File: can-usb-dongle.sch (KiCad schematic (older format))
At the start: 42 parts, among them SW1 SW_PUSH, U1 STM32F302C8T, U2 SN65HVD256, U3 NUF2042XV6, U4 MCP1700, U5 SiP32431, X1 16MHz 10ppm

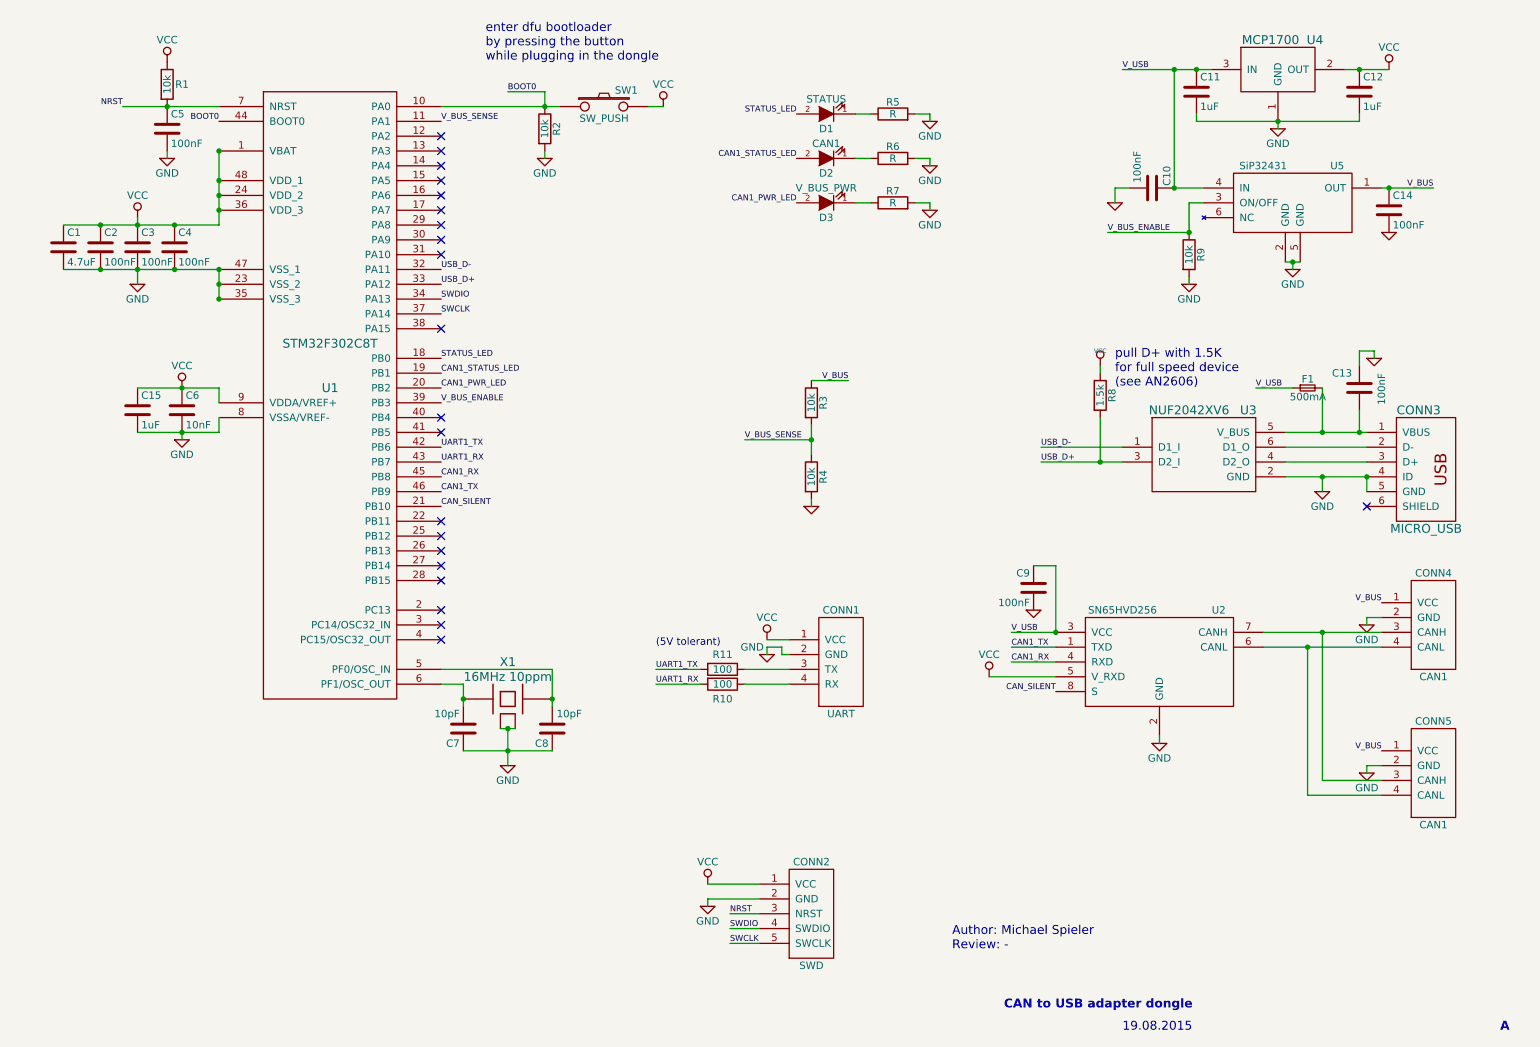
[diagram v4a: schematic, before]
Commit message: Change pinout to optimize routing.
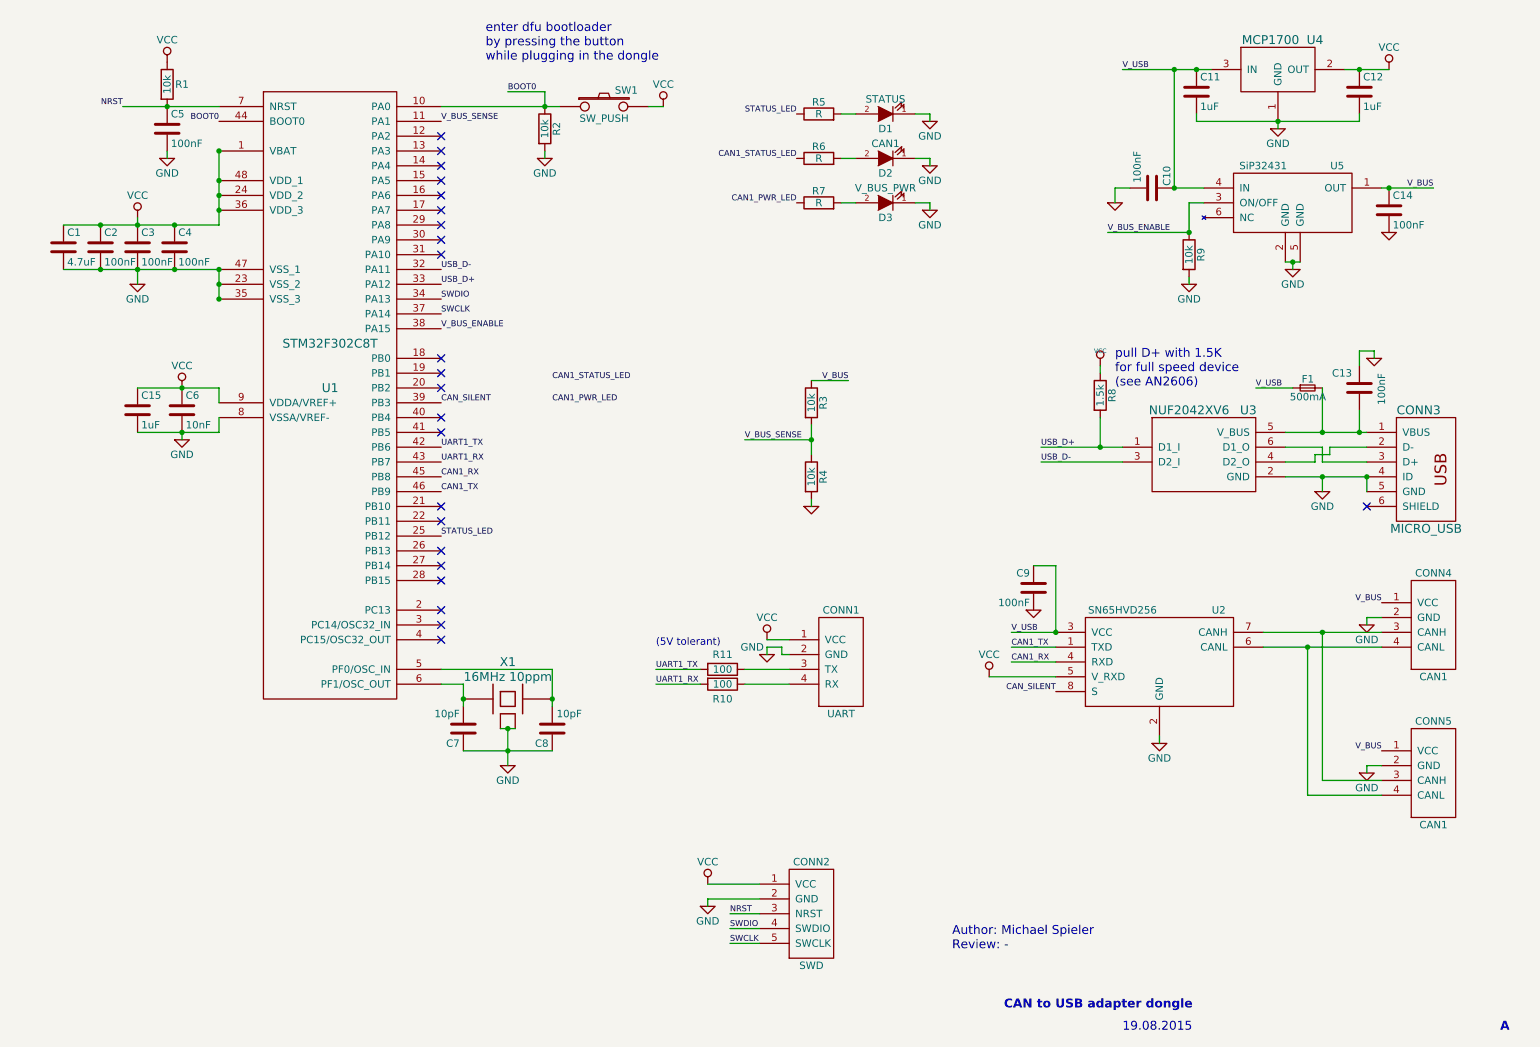
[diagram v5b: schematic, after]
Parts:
- CONN3: footprint _connectors:_Micro-USB-AB-receptacle-SMT-th -> _connectors:_Micro-USB-AB-receptacle-SMT-th-no-slot
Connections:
- net CAN1_PWR_LED: now also R7.1; no longer D3.2 (A), U1.20 (PB2)
- net CAN1_STATUS_LED: now also R6.1; no longer D2.2 (A), U1.19 (PB1)
- net CAN_SILENT: now also U1.39 (PB3); no longer U1.21 (PB10)
- net GND: now also D1.1 (K), D2.1 (K), D3.1 (K); no longer R5.2, R6.2, R7.2
- net STATUS_LED: now also R5.1, U1.25 (PB12); no longer D1.2 (A), U1.18 (PB0)
- net USB_D+: now also U3.1 (D1_I); no longer U3.3 (D2_I)
- net USB_D-: now also U3.3 (D2_I); no longer U3.1 (D1_I)
- net V_BUS_ENABLE: now also U1.38 (PA15); no longer U1.39 (PB3)
- net at CONN3.2 (D-): now also U3.4 (D2_O); no longer U3.6 (D1_O)
- net at CONN3.3 (D+): now also U3.6 (D1_O); no longer U3.4 (D2_O)
- new net: D2.2 (A), R6.2
- new net: D1.2 (A), R5.2
- new net: D3.2 (A), R7.2
- no-connect marks 21 -> 23
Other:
- moved on the sheet: D1, D2, D3, R5, R6, R7
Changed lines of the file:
@@
 Text Label 3600 2600 0    40   ~ 0
 USB_D+
+Text Label 7650 3800 0    40   ~ 0
+USB_D-
 Text Label 7650 3700 0    40   ~ 0
-USB_D-
-Text Label 7650 3800 0    40   ~ 0
 USB_D+
 Text Label 9100 3300 0    40   ~ 0
@@
 L R R6
 U 1 1 55622F4C
-P 6650 1750
-F 0 "R6" V 6730 1750 50  0000 C CNN
-F 1 "R" V 6650 1750 50  0000 C CNN
-F 2 "_std:_0603" V 6580 1750 30  0001 C CNN
-F 3 "" H 6650 1750 30  0000 C CNN
-	1    6650 1750
+P 6150 1750
+F 0 "R6" V 6230 1750 50  0000 C CNN
+F 1 "R" V 6150 1750 50  0000 C CNN
+F 2 "_std:_0603" V 6080 1750 30  0001 C CNN
+F 3 "" H 6150 1750 30  0000 C CNN
+	1    6150 1750
 	0    -1   -1   0
 $EndComp
@@
 L LED D1
 U 1 1 55624274
-P 6200 1450
-F 0 "D1" H 6200 1550 50  0000 C CNN
-F 1 "STATUS" H 6200 1350 50  0000 C CNN
-F 2 "_std:_0603" H 6200 1450 60  0001 C CNN
-F 3 "" H 6200 1450 60  0000 C CNN
-	1    6200 1450
+P 6600 1450
+F 0 "D1" H 6600 1550 50  0000 C CNN
+F 1 "STATUS" H 6600 1350 50  0000 C CNN
+F 2 "_std:_0603" H 6600 1450 60  0001 C CNN
+F 3 "" H 6600 1450 60  0000 C CNN
+	1    6600 1450
 	-1   0    0    1
 $EndComp
@@
 L R R5
 U 1 1 5562427A
-P 6650 1450
-F 0 "R5" V 6730 1450 50  0000 C CNN
-F 1 "R" V 6650 1450 50  0000 C CNN
-F 2 "_std:_0603" V 6580 1450 30  0001 C CNN
-F 3 "" H 6650 1450 30  0000 C CNN
-	1    6650 1450
+P 6150 1450
+F 0 "R5" V 6230 1450 50  0000 C CNN
+F 1 "R" V 6150 1450 50  0000 C CNN
+F 2 "_std:_0603" V 6080 1450 30  0001 C CNN
+F 3 "" H 6150 1450 30  0000 C CNN
+	1    6150 1450
 	0    -1   -1   0
 $EndComp
@@
 Text Label 6000 1450 2    40   ~ 0
 STATUS_LED
-Text Label 3600 3200 0    40   ~ 0
+Text Label 4350 3250 0    40   ~ 0
 CAN1_STATUS_LED
 $Comp
 L LED D2
 U 1 1 55622E77
-P 6200 1750
-F 0 "D2" H 6200 1850 50  0000 C CNN
-F 1 "CAN1" H 6200 1650 50  0000 C CNN
-F 2 "_std:_0603" H 6200 1750 60  0001 C CNN
-F 3 "" H 6200 1750 60  0000 C CNN
-	1    6200 1750
+P 6600 1750
+F 0 "D2" H 6600 1850 50  0000 C CNN
+F 1 "CAN1" H 6600 1650 50  0000 C CNN
+F 2 "_std:_0603" H 6600 1750 60  0001 C CNN
+F 3 "" H 6600 1750 60  0000 C CNN
+	1    6600 1750
 	-1   0    0    1
 $EndComp
@@
 	1    0    0    -1
 $EndComp
-Text Label 7450 4950 0    40   ~ 0
-V_USB
 $Comp
 L VCC #PWR018
@@
 	1    0    0    -1
 $EndComp
-Text Label 3600 4100 0    40   ~ 0
+Text Label 3600 3400 0    40   ~ 0
 CAN_SILENT
 Text Label 3600 3800 0    40   ~ 0
@@
 Text Label 3600 3700 0    40   ~ 0
 UART1_TX
-Text Label 3600 3100 0    40   ~ 0
+Text Label 3600 4300 0    40   ~ 0
 STATUS_LED
 Text Notes 3900 1100 0    60   ~ 0
@@
 Text Label 8100 2250 0    40   ~ 0
 V_BUS_ENABLE
-Text Label 3600 3400 0    40   ~ 0
+Text Label 3600 2900 0    40   ~ 0
 V_BUS_ENABLE
 $Comp
@@
 L LED D3
 U 1 1 560BDA9A
-P 6200 2050
-F 0 "D3" H 6200 2150 50  0000 C CNN
-F 1 "V_BUS_PWR" H 6200 1950 50  0000 C CNN
-F 2 "_std:_0603" H 6200 2050 60  0001 C CNN
-F 3 "" H 6200 2050 60  0000 C CNN
-	1    6200 2050
+P 6600 2050
+F 0 "D3" H 6600 2150 50  0000 C CNN
+F 1 "V_BUS_PWR" H 6600 1950 50  0000 C CNN
+F 2 "_std:_0603" H 6600 2050 60  0001 C CNN
+F 3 "" H 6600 2050 60  0000 C CNN
+	1    6600 2050
 	-1   0    0    1
 $EndComp
@@
 L R R7
 U 1 1 560BDAA0
-P 6650 2050
-F 0 "R7" V 6730 2050 50  0000 C CNN
-F 1 "R" V 6650 2050 50  0000 C CNN
-F 2 "_std:_0603" V 6580 2050 30  0001 C CNN
-F 3 "" H 6650 2050 30  0000 C CNN
-	1    6650 2050
+P 6150 2050
+F 0 "R7" V 6230 2050 50  0000 C CNN
+F 1 "R" V 6150 2050 50  0000 C CNN
+F 2 "_std:_0603" V 6080 2050 30  0001 C CNN
+F 3 "" H 6150 2050 30  0000 C CNN
+	1    6150 2050
 	0    -1   -1   0
 $EndComp
@@
 F 0 "CONN3" H 10200 4250 60  0000 C CNN
 F 1 "MICRO_USB" H 10250 3450 60  0000 C CNN
-F 2 "_connectors:_Micro-USB-AB-receptacle-SMT-th" H 10200 3850 60  0001 C CNN
+F 2 "_connectors:_Micro-USB-AB-receptacle-SMT-th-no-slot" H 10200 3850 60  0001 C CNN
 F 3 "" H 10200 3850 60  0000 C CNN
 	1    10200 3850
@@
 pull D+ with 1.5K\nfor full speed device\n(see AN2606)
 NoConn ~ 3600 5000
-NoConn ~ 3600 4900
-NoConn ~ 3600 4800
 NoConn ~ 3600 4600
 NoConn ~ 3600 4500
 NoConn ~ 3600 4400
-NoConn ~ 3600 4300
 NoConn ~ 3600 4200
 NoConn ~ 3600 3600
 NoConn ~ 3600 3500
-NoConn ~ 3600 2900
+NoConn ~ 3600 4100
 NoConn ~ 3600 2200
 NoConn ~ 3600 2100
@@
 Wire Wire Line
 	6800 1450 6900 1450
-Wire Wire Line
-	6400 1450 6500 1450
 Connection ~ 4300 1400
 Wire Wire Line
@@
 Connection ~ 2100 1700
 Wire Wire Line
-	6400 1750 6500 1750
-Wire Wire Line
 	6800 1750 6900 1750
 Wire Wire Line
@@
 	6800 2050 6900 2050
 Wire Wire Line
-	6400 2050 6500 2050
-Wire Wire Line
 	6900 2050 6900 2100
 Wire Wire Line
@@
 	6350 3250 6100 3250
 Wire Wire Line
+	7650 3800 8200 3800
+Wire Wire Line
 	7650 3700 8200 3700
-Wire Wire Line
-	9300 3700 9850 3700
-Wire Wire Line
-	9300 3800 9850 3800
-Wire Wire Line
-	7650 3800 8200 3800
 Connection ~ 9800 3600
 Wire Wire Line
@@
 Connection ~ 9550 3600
 Connection ~ 9550 3900
-Connection ~ 8050 3800
-Wire Wire Line
-	8050 3500 8050 3800
 Wire Wire Line
 	7600 4500 7750 4500
@@
 Text Label 6000 2050 2    40   ~ 0
 CAN1_PWR_LED
-Text Label 3600 3300 0    40   ~ 0
+Text Label 4350 3400 0    40   ~ 0
 CAN1_PWR_LED
 Text Label 6000 1750 2    40   ~ 0
@@
 	1    0    0    -1
 $EndComp
+Wire Wire Line
+	8050 3500 8050 3700
+Connection ~ 8050 3700
+Wire Wire Line
+	9300 3700 9550 3700
+Wire Wire Line
+	9550 3700 9550 3800
+Wire Wire Line
+	9550 3800 9850 3800
+Wire Wire Line
+	9850 3700 9600 3700
+Wire Wire Line
+	9600 3700 9600 3750
+Wire Wire Line
+	9600 3750 9500 3750
+Wire Wire Line
+	9500 3750 9500 3800
+Wire Wire Line
+	9500 3800 9300 3800
+Wire Wire Line
+	6300 1750 6400 1750
+Wire Wire Line
+	6300 1450 6400 1450
+Wire Wire Line
+	6300 2050 6400 2050
+NoConn ~ 3600 3300
+NoConn ~ 3600 3200
+NoConn ~ 3600 3100
+NoConn ~ 3600 4800
+NoConn ~ 3600 4900
+Text Label 7450 4950 0    40   ~ 0
+V_USB
 $EndSCHEMATC

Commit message: All components roughly placed.
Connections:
- net CAN1_PWR_LED: now also U1.41 (PB5)
- net CAN1_STATUS_LED: now also U1.40 (PB4)
- net V_BUS renamed V_CAN_BUS
- no-connect marks 23 -> 21
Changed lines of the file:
@@
 Text Label 6000 1450 2    40   ~ 0
 STATUS_LED
-Text Label 4350 3250 0    40   ~ 0
+Text Label 3600 3500 0    40   ~ 0
 CAN1_STATUS_LED
 $Comp
@@
 $EndComp
 Text Label 9950 4750 2    40   ~ 0
-V_BUS
+V_CAN_BUS
 $Comp
 L VCC #PWR016
@@
 	1    0    0    -1
 $EndComp
-Text Label 10300 1950 2    40   ~ 0
-V_BUS
+Text Label 10450 1950 2    40   ~ 0
+V_CAN_BUS
 $Comp
 L GND-RESCUE-can-usb-dongle #PWR022
@@
 $EndComp
 Text Label 9950 5750 2    40   ~ 0
-V_BUS
+V_CAN_BUS
 $Comp
 L GND-RESCUE-can-usb-dongle #PWR024
@@
 	1    0    0    -1
 $EndComp
-Text Label 6350 3250 2    40   ~ 0
-V_BUS
+Text Label 6450 3250 2    40   ~ 0
+V_CAN_BUS
 $Comp
 L R R3
@@
 NoConn ~ 3600 4400
 NoConn ~ 3600 4200
-NoConn ~ 3600 3600
-NoConn ~ 3600 3500
 NoConn ~ 3600 4100
 NoConn ~ 3600 2200
@@
 Connection ~ 8550 1150
 Wire Wire Line
-	9950 1950 10300 1950
+	9950 1950 10450 1950
 Wire Wire Line
 	9300 2450 9400 2450
@@
 	6100 4100 6100 4050
 Wire Wire Line
-	6350 3250 6100 3250
+	6450 3250 6100 3250
 Wire Wire Line
 	7650 3800 8200 3800
@@
 Text Label 6000 2050 2    40   ~ 0
 CAN1_PWR_LED
-Text Label 4350 3400 0    40   ~ 0
+Text Label 3600 3600 0    40   ~ 0
 CAN1_PWR_LED
 Text Label 6000 1750 2    40   ~ 0
@@
 Connection ~ 8050 3700
 Wire Wire Line
-	9300 3700 9550 3700
-Wire Wire Line
-	9550 3700 9550 3800
-Wire Wire Line
-	9550 3800 9850 3800
+	9300 3700 9500 3700
+Wire Wire Line
+	9500 3700 9600 3800
+Wire Wire Line
+	9600 3800 9850 3800
 Wire Wire Line
 	9850 3700 9600 3700
 Wire Wire Line
-	9600 3700 9600 3750
-Wire Wire Line
-	9600 3750 9500 3750
-Wire Wire Line
-	9500 3750 9500 3800
+	9600 3700 9500 3800
 Wire Wire Line
 	9500 3800 9300 3800

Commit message: Optimize VCC routing, redo power supply.
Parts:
- F1: footprint _std:_0603 -> Resistors_SMD:R_0805
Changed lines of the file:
@@
 F 0 "F1" H 9410 3360 50  0000 L CNN
 F 1 "500mA" H 9330 3240 50  0000 L CNN
-F 2 "_std:_0603" H 9450 3300 60  0001 C CNN
+F 2 "Resistors_SMD:R_0805" H 9450 3300 60  0001 C CNN
 F 3 "" H 9450 3300 60  0000 C CNN
 	1    9450 3300

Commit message: Update footprints (USB, voltage regulator)
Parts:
- CONN3: footprint _connectors:_Micro-USB-AB-receptacle-SMT-th-no-slot -> _connectors:_Micro-USB-AB-receptacle-SMT-th
- U4: footprint Housings_SOT-23_SOT-143_TSOT-6:SOT-23 -> _std:SOT-23
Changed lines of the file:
@@
 F 0 "U4" H 9500 1350 60  0000 C CNN
 F 1 "MCP1700" H 9200 1350 60  0000 C CNN
-F 2 "Housings_SOT-23_SOT-143_TSOT-6:SOT-23" H 9150 1600 60  0001 C CNN
+F 2 "_std:SOT-23" H 9150 1600 60  0001 C CNN
 F 3 "" H 9150 1600 60  0000 C CNN
 	1    9250 1150
@@
 F 0 "CONN3" H 10200 4250 60  0000 C CNN
 F 1 "MICRO_USB" H 10250 3450 60  0000 C CNN
-F 2 "_connectors:_Micro-USB-AB-receptacle-SMT-th-no-slot" H 10200 3850 60  0001 C CNN
+F 2 "_connectors:_Micro-USB-AB-receptacle-SMT-th" H 10200 3850 60  0001 C CNN
 F 3 "" H 10200 3850 60  0000 C CNN
 	1    10200 3850
